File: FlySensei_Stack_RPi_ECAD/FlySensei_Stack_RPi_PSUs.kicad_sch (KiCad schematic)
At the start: 28 parts, among them SW3 SW_SPDT, U16 AP64501SP-13, U7 MPM3610

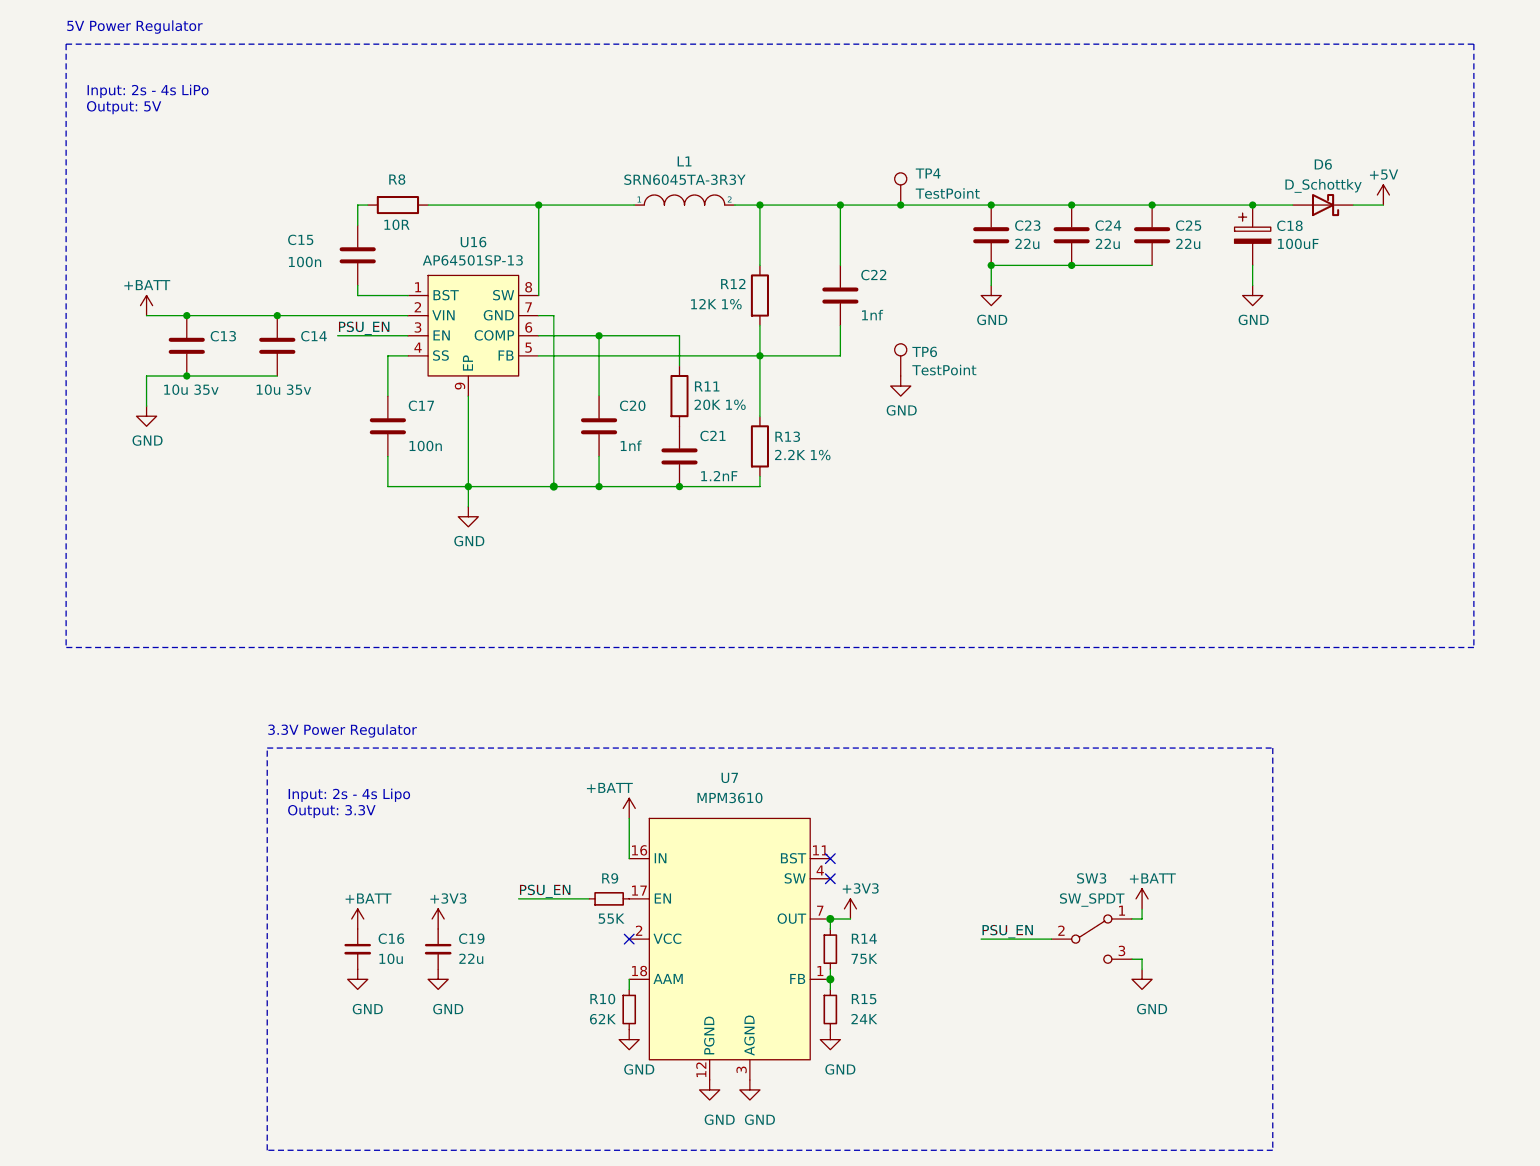
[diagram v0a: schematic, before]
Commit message: PCB Design for the Raspberry PI CM4 Board (V0.1)
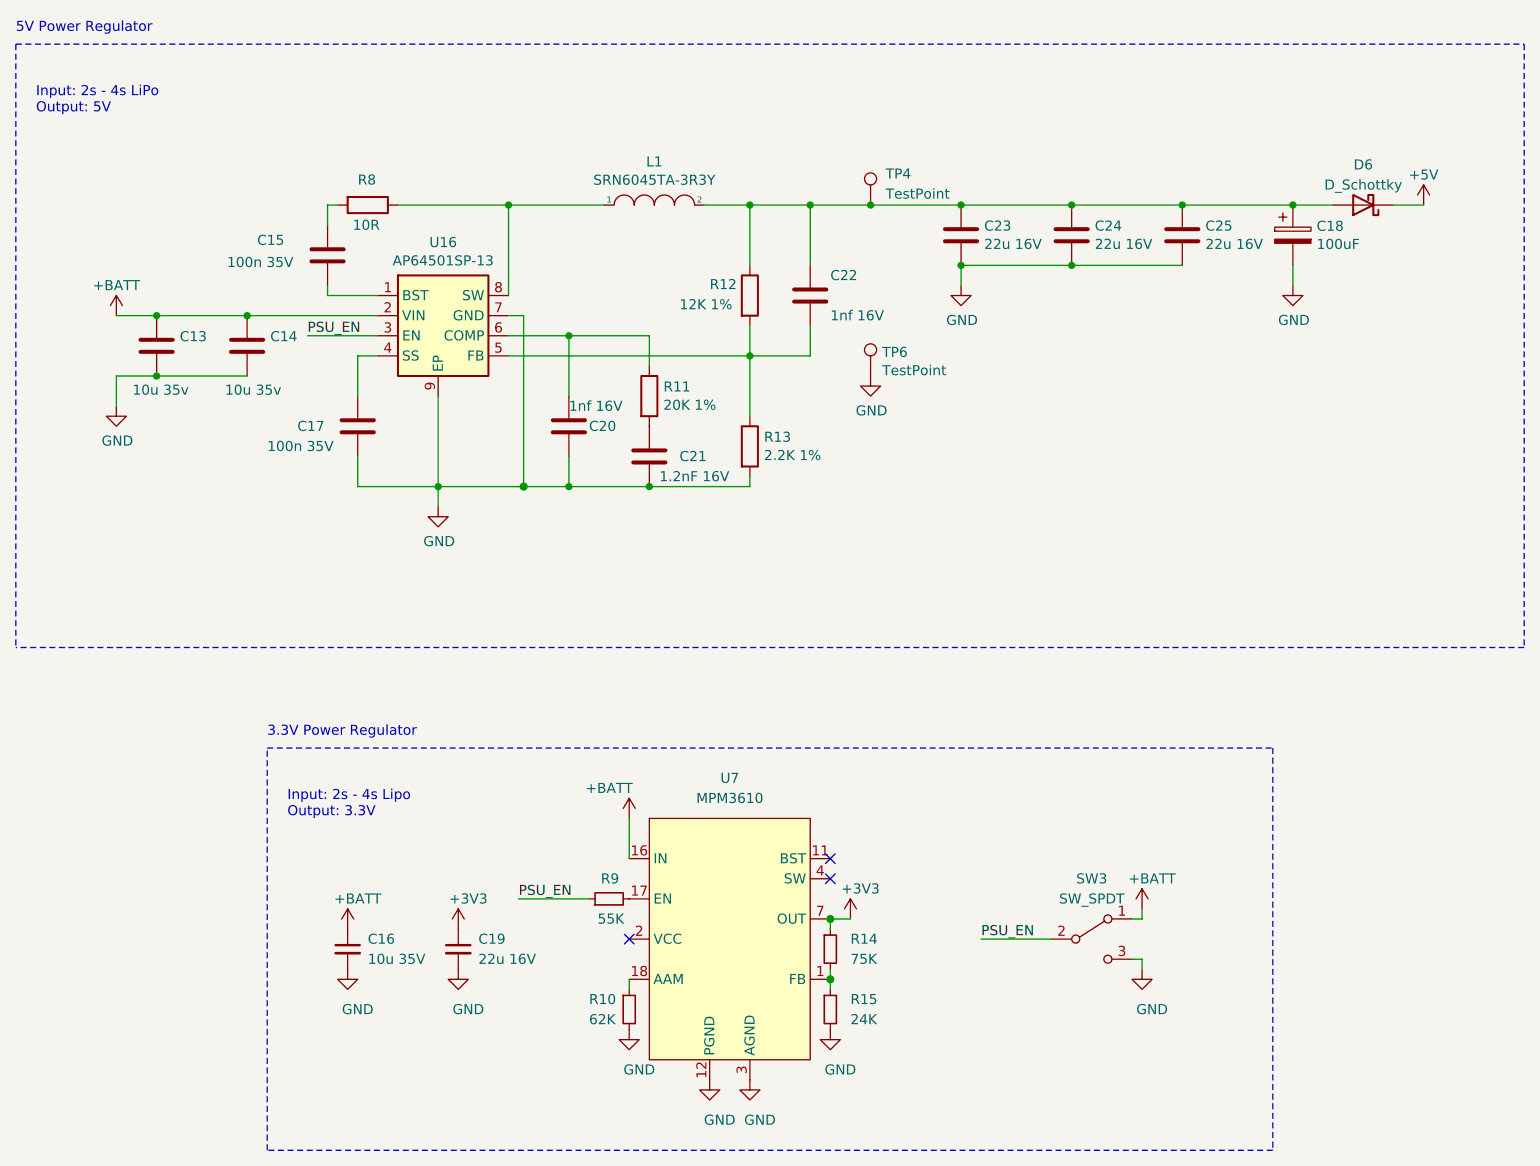
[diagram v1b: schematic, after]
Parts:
- C15, C17: value 100n -> 100n 35V
- C16: value 10u -> 10u 35V
- C19, C23, C24, C25: value 22u -> 22u 16V
- C20, C22: value 1nf -> 1nf 16V
- C21: value 1.2nF -> 1.2nF 16V
- D6: footprint (none) -> Diode_SMD:D_SMB
- U16: symbol CM4IO:AP64351 -> RPi_CM4IO:AP64351
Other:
- moved on the sheet: C13, C14, C15, C16, C17, C18, C19, C20, C21, C22, C23, C25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

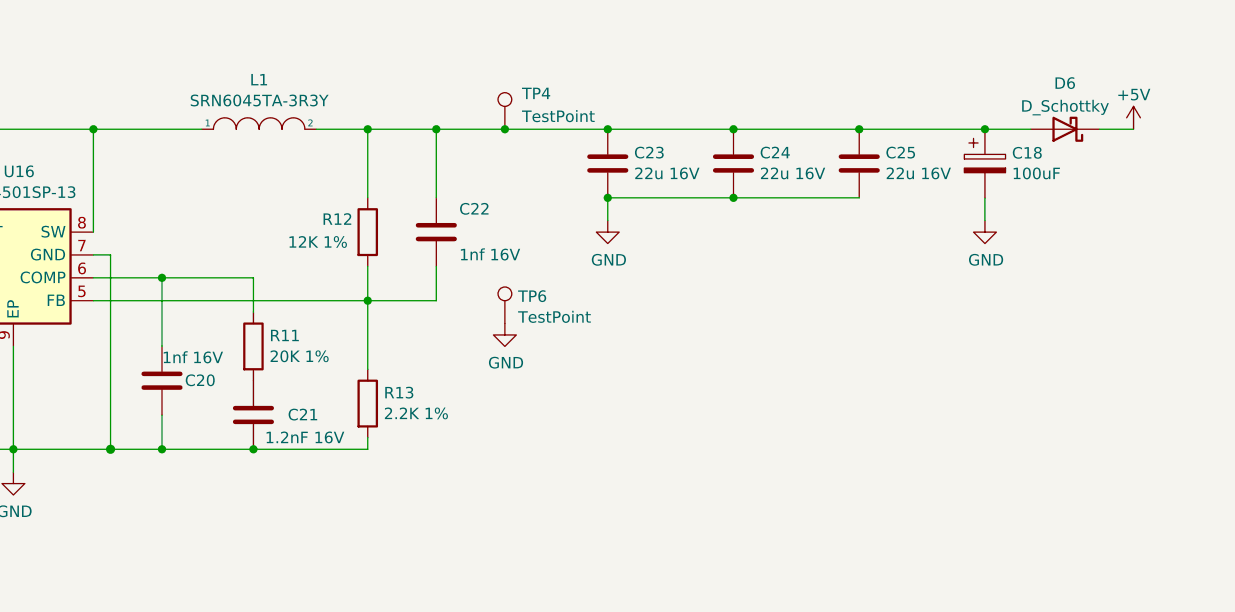
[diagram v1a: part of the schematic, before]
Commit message: Cleanup component values to remain consistent in all skeets
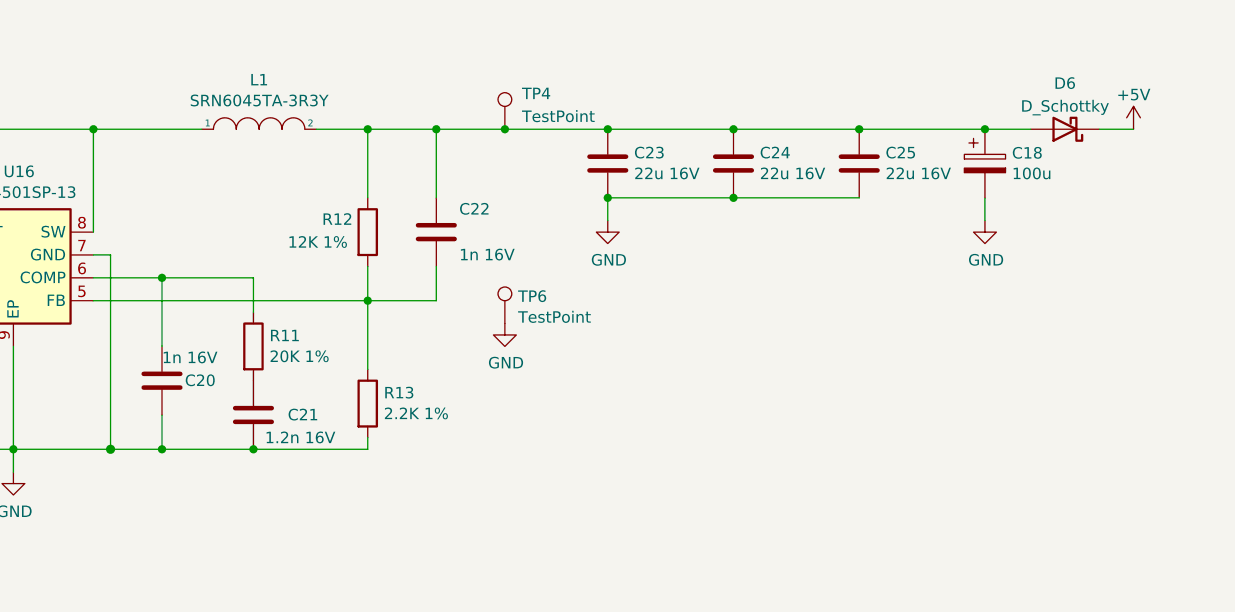
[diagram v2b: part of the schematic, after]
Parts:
- C18: value 100uF -> 100u
- C20, C22: value 1nf 16V -> 1n 16V
- C21: value 1.2nF 16V -> 1.2n 16V
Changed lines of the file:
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@@
       (effects (font (size 1.27 1.27)) (justify left))
     )
-    (property "Value" "1nf 16V" (id 1) (at 114.3 71.12 0)
+    (property "Value" "1n 16V" (id 1) (at 114.3 71.12 0)
       (effects (font (size 1.27 1.27)) (justify left))
     )
@@
       (effects (font (size 1.27 1.27)) (justify left))
     )
-    (property "Value" "1.2nF 16V" (id 1) (at 125.73 80.01 0)
+    (property "Value" "1.2n 16V" (id 1) (at 125.73 80.01 0)
       (effects (font (size 1.27 1.27)) (justify left))
     )
@@
       (effects (font (size 1.27 1.27)) (justify left))
     )
-    (property "Value" "1nf 16V" (id 1) (at 147.32 59.69 0)
+    (property "Value" "1n 16V" (id 1) (at 147.32 59.69 0)
       (effects (font (size 1.27 1.27)) (justify left))
     )
@@
       (effects (font (size 1.27 1.27)) (justify left))
     )
-    (property "Value" "100uF" (id 1) (at 208.7372 50.673 0)
-      (effects (font (size 1.27 1.27)) (justify left))
-    )
+    (property "Value" "100u" (id 1) (at 208.7372 50.673 0)
+      (effects (font (size 1.27 1.27)) (justify left))
+    )
